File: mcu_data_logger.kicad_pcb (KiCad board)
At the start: 2 copper layers, 50.2 x 37.3 mm, 30 parts, among them J1 Conn_01x04_Pin, J2 Conn_01x09_Pin, J3 Conn_01x04_Pin, J4 Conn_02x03_Odd_Even, U1 24LC1025, U2 DS1337S_, U3 24LC1025, U4 ATMEGA328P-AU, Y1 32.768 kHz, Y2 16MHz

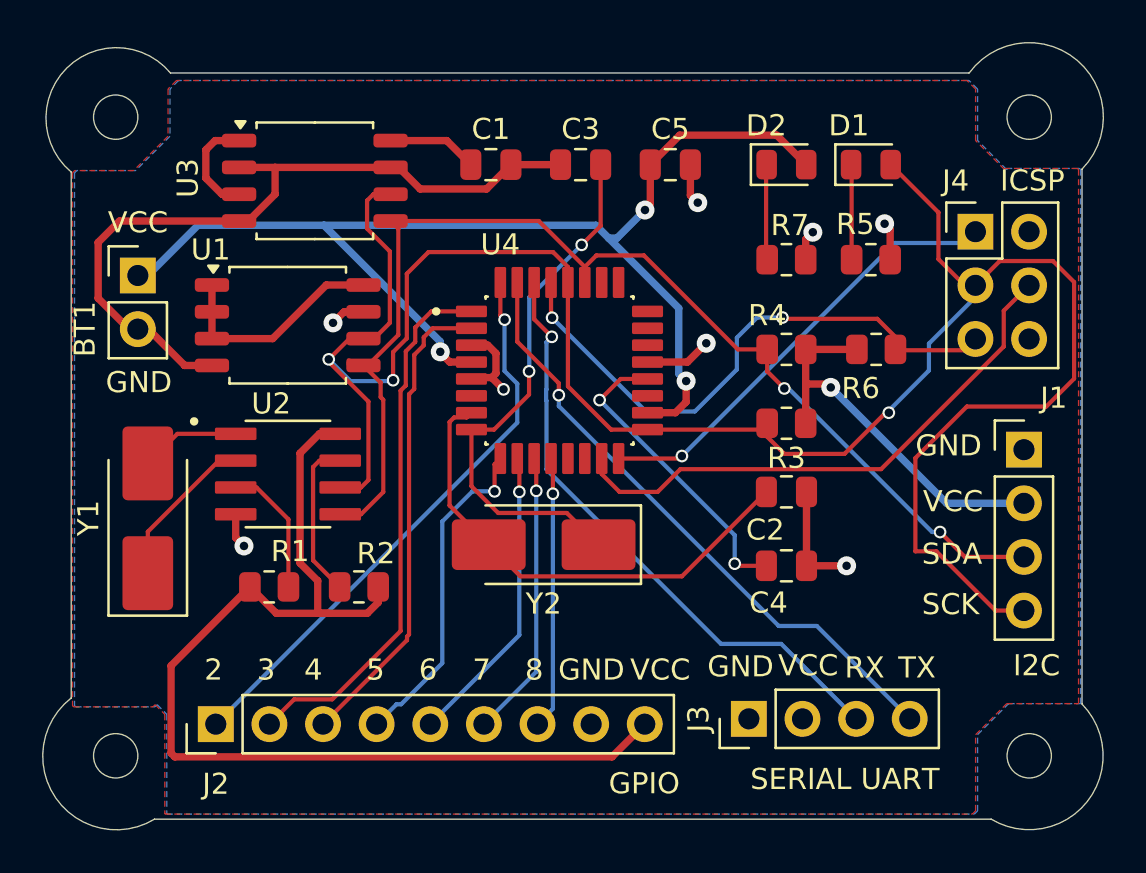
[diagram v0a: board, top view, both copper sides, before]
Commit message: 4-layer routing complete
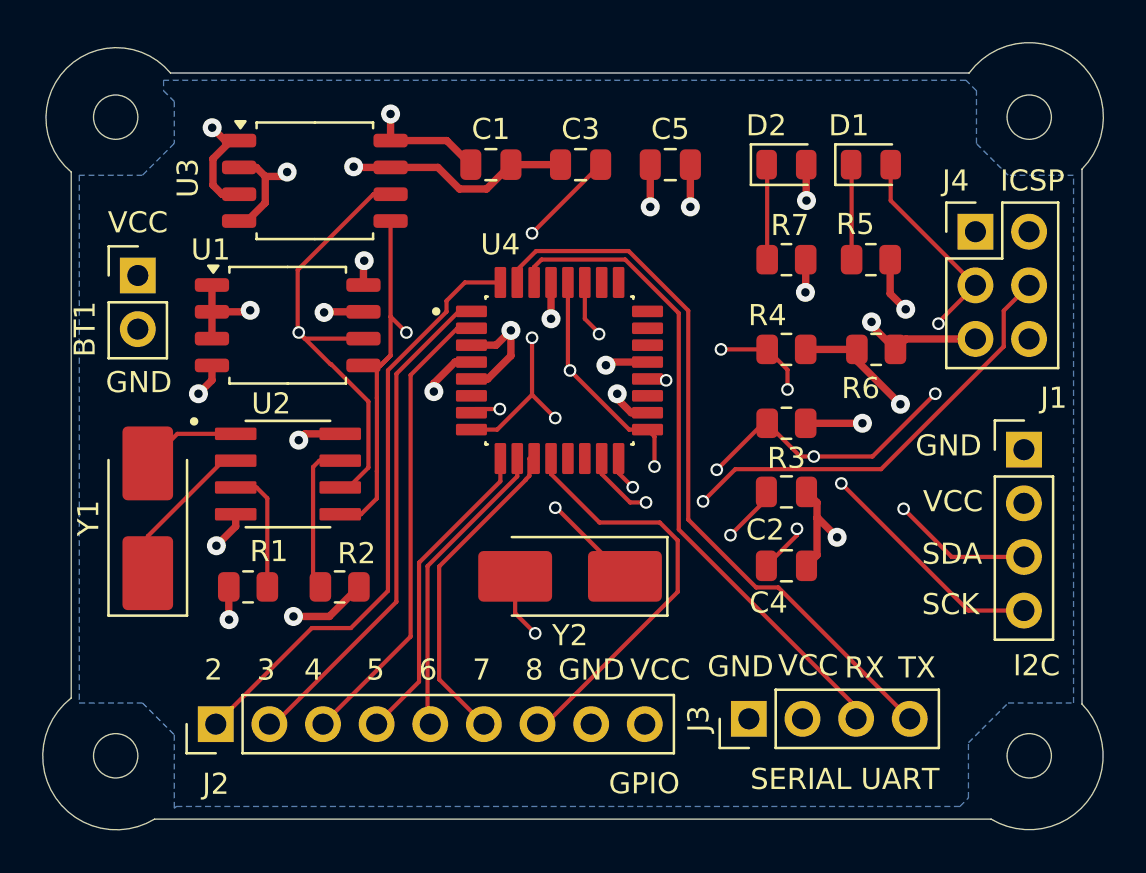
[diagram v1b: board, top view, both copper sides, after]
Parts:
- moved Y2 1.95 mm to (95.2, 81.5)
- moved R1 1.00 mm to (80.0, 82.0)
- moved R2 0.91 mm to (84.3, 82.0)
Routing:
- net /Vcc: track 148.4 -> 41.0 mm, vias 4 -> 13
- net /SCK: track 105.8 -> 88.5 mm, vias 3 -> 8
- net GND: track 57.5 -> 40.6 mm, vias 8 -> 11
- net /D8: track 12.9 -> 19.7 mm, vias 1 -> 0
- net Net-(U4-PB6): track 23.2 -> 29.8 mm, vias 0 -> 3
- net /TX: track 29.4 -> 34.5 mm, vias 1 -> 0
- net /RESET: track 27.5 -> 22.7 mm
- net /RX: track 28.9 -> 31.5 mm, vias 1 -> 0
- net /MISO: track 21.4 -> 23.9 mm
- net /D7: track 13.6 -> 15.5 mm, vias 1 -> 0
- net Net-(U4-AREF): track 14.6 -> 12.9 mm
- net /D3: track 25.7 -> 24.0 mm
- net /D2: track 27.3 -> 28.6 mm, vias 1 -> 0
- net /D4: track 23.0 -> 22.1 mm
- net Net-(U2-SQW/~INT): track 7.99 -> 7.23 mm
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- added copper zone on In1.Cu, net /Vcc
- removed copper zone on F.Cu, net /Vcc
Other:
- copper layers 2 -> 4

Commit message: fixed 4layer routing after fixing the schematic
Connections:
- J1 pad 4: /SCK -> /SCL
- R3 pad 2: /SCK -> /SCL
- U1 pad 6: /SCK -> /SCL
- U2 pad 6: /SCK -> /SCL
- U3 pad 6: /SCK -> /SCL
- U4 pad 28: /SCK -> /SCL
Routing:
- net /SCL: track 0.00 -> 77.8 mm, vias 0 -> 3
- net /SCK: track 88.5 -> 30.0 mm, vias 8 -> 4
